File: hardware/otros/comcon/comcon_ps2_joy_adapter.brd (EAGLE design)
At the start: 50 x 50 mm, 44 parts

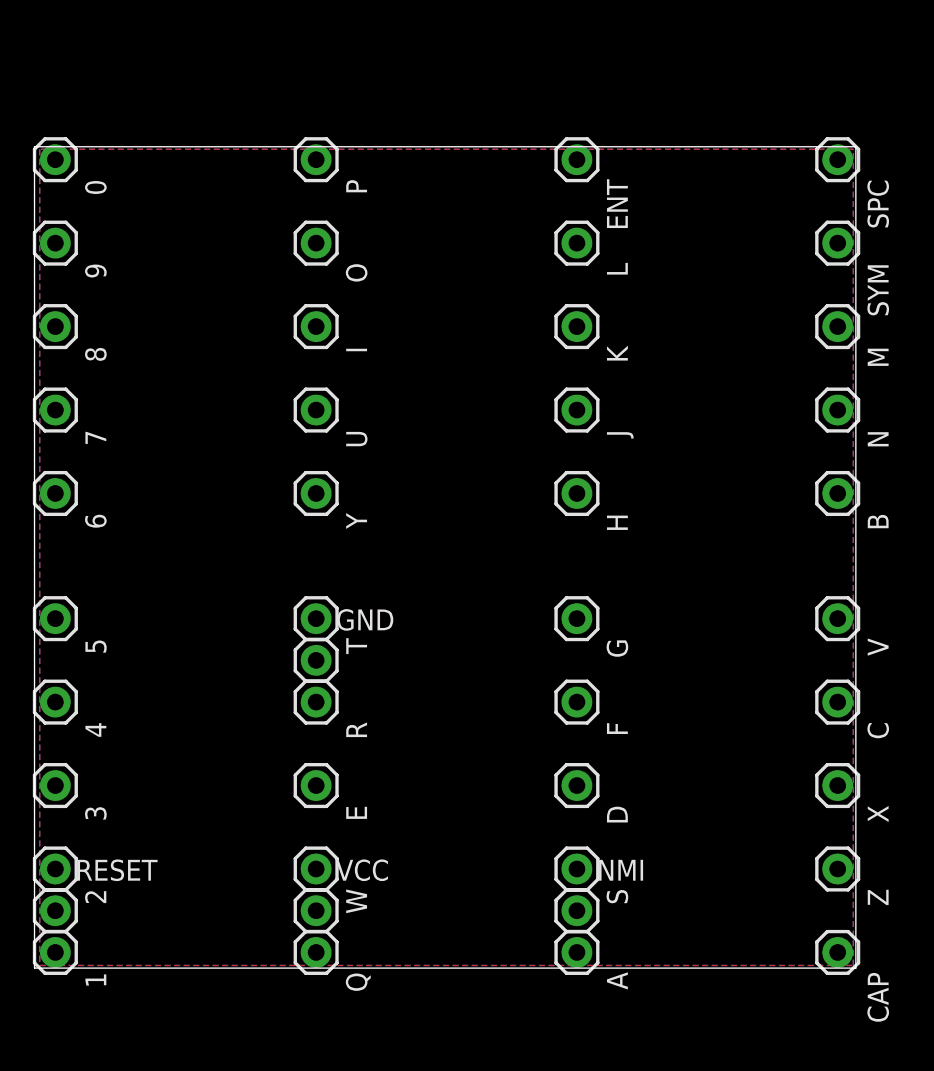
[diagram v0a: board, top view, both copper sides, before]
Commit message: 
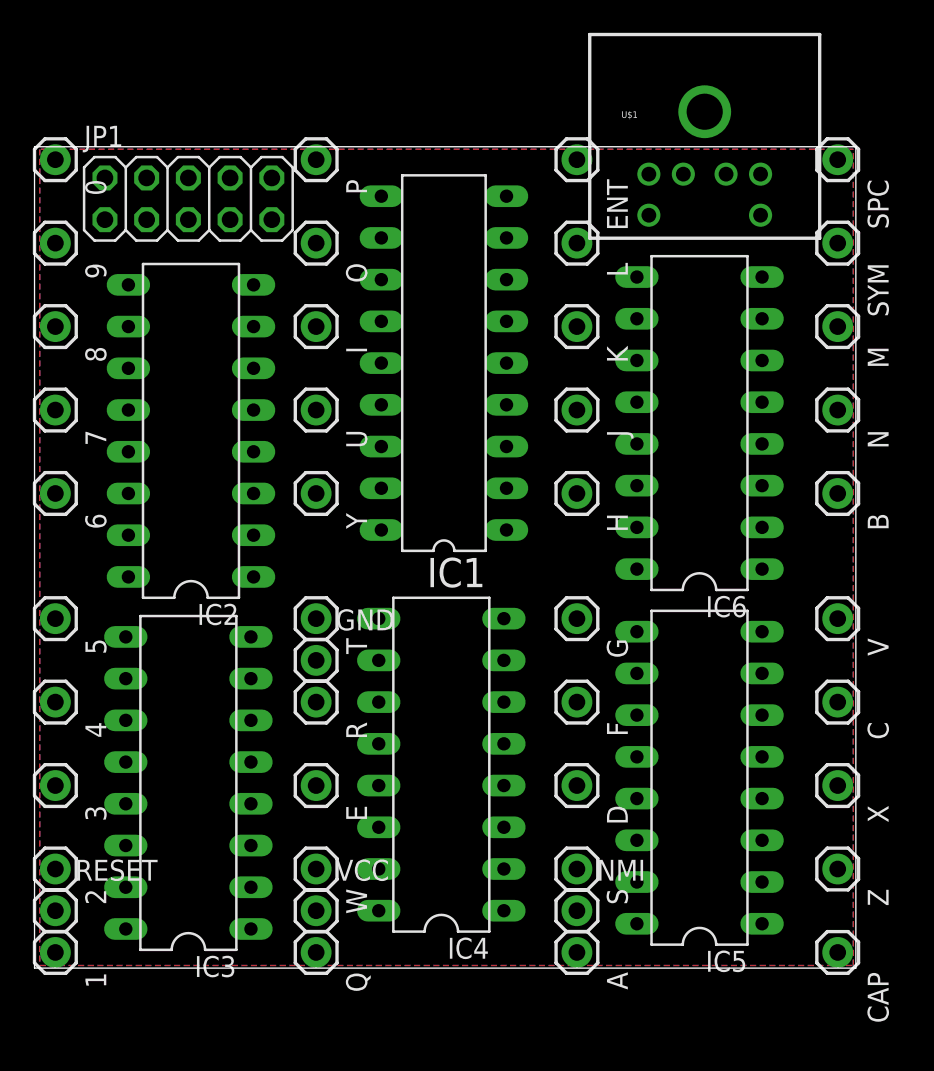
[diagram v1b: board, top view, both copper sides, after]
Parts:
- added IC1: PIC16F628P, microchip:DIL18
- added IC2, IC3, IC4, IC5, IC6: 74HC595N, 74xx-eu:DIL16
- added JP1: (no value), pinhead:2X05
- added U$1: MINI-DIN6PTH, SparkFun-Connectors:MINI-DIN6
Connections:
- removed net N$63: A.1
- removed net N$64: S.1
- new net N$1: A.1, IC2.5
- new net N$3: IC2.6, S.1
- new net N$4: IC2.9, IC3.14
- new net N$5: IC5.9, IC6.14
- new net N$6: IC3.9, IC4.14
- new net N$7: IC4.9, IC5.14
- new net VDD: IC1.14
- new net VSS: IC1.5
- net GND: now also IC2.8, IC3.8, IC4.8, IC5.8, IC6.8
- net N$105: now also IC4.15
- net N$106: now also IC4.1
- net N$107: now also IC4.2
- net N$108: now also IC4.3
- net N$12: now also IC6.1
- net N$18: now also IC6.2
- net N$2: now also IC6.15; no longer SPC.1
- net N$20: now also IC6.3
- net N$22: now also IC6.4
- net N$25: now also IC2.15
- net N$26: now also IC2.1
- net N$27: now also IC2.2
- net N$28: now also IC2.3
- net N$47: now also IC2.4
- net N$55: now also IC6.7
- net N$65: now also IC2.7
- net N$74: now also IC5.2; no longer P.1
- net N$75: now also IC5.3
- net N$76: now also IC5.4
- net N$77: now also IC5.5
- net N$78: now also IC5.6
- net N$84: now also IC3.2; no longer Q.1
- net N$85: now also IC3.3
- net N$86: now also IC3.4
- net N$87: now also IC3.5
- net N$88: now also IC3.6
- net N$94: now also IC5.7
- net N$95: now also IC4.7
- net N$96: now also IC4.6
- net N$97: now also IC4.5
- net N$98: now also IC4.4
- net VCC: now also IC2.16, IC3.16, IC4.16, IC5.16, IC6.16

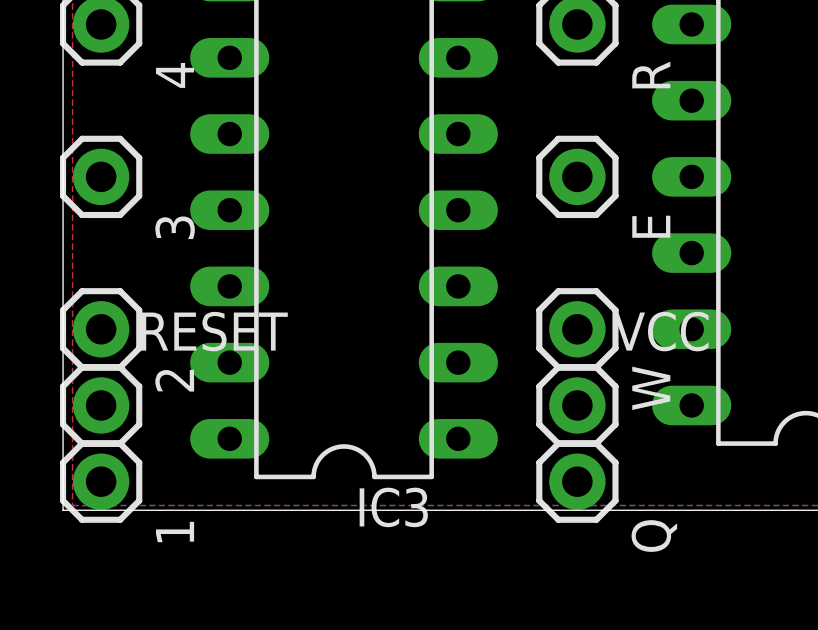
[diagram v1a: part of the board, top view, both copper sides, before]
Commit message: 
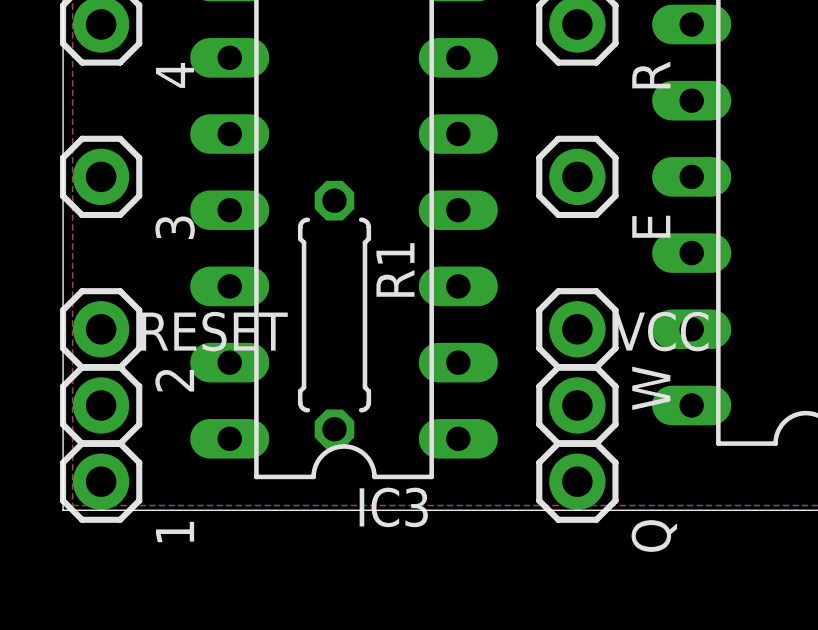
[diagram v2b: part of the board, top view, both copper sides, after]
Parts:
- added R1: 4K7, resistor:0207/7
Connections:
- removed net VSS: IC1.5
- new net N$8: IC1.4, JP1.1, R1.1
- new net RA0: IC2.12, IC3.12, IC4.12, IC5.12, IC6.12
- new net RA1: IC2.11, IC3.11, IC4.11, IC5.11, IC6.11
- new net RA2: IC2.14
- new net RB6: IC1.12
- new net RB7: IC1.13
- net GND: now also IC1.5, IC2.13, IC3.13, IC4.13, IC5.13, IC6.13, JP1.5
- net N$104: now also IC3.7
- net N$53: now also IC6.5
- net N$54: now also IC6.6
- net N$56: now also IC5.15
- net N$57: now also IC5.1
- net N$66: now also IC3.15
- net N$67: now also IC3.1
- net VCC: now also IC2.10, IC3.10, IC4.10, IC5.10, IC6.10, JP1.3, R1.2
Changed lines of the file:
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@@
 <element name="U$1" library="SparkFun-Connectors" package="MINI-DIN6" value="MINI-DIN6PTH" x="40.79875" y="56.8325"/>
 <element name="JP1" library="pinhead" package="2X05" value="" x="9.36625" y="46.83125"/>
+<element name="R1" library="resistor" package="0207/7" value="4K7" x="9.04875" y="6.50875" rot="R270"/>
 </elements>
 <signals>
@@
 <contactref element="IC5" pad="8"/>
 <contactref element="IC6" pad="8"/>
-<wire x1="44.29125" y1="20.47875" x2="44.29125" y2="42.06875" width="0" layer="19" extent="1-1"/>
-<wire x1="28.575" y1="21.2725" x2="44.29125" y2="20.47875" width="0" layer="19" extent="1-1"/>
-<wire x1="13.17625" y1="20.16125" x2="28.575" y2="21.2725" width="0" layer="19" extent="1-1"/>
-<wire x1="13.335" y1="41.5925" x2="13.17625" y2="20.16125" width="0" layer="19" extent="1-1"/>
-<wire x1="17.145" y1="18.7325" x2="13.335" y2="41.5925" width="0" layer="19" extent="1-1"/>
+<contactref element="IC3" pad="13"/>
+<contactref element="IC4" pad="13"/>
+<contactref element="IC5" pad="13"/>
+<contactref element="IC6" pad="13"/>
+<contactref element="IC2" pad="13"/>
+<contactref element="IC1" pad="5"/>
+<contactref element="JP1" pad="5"/>
+<wire x1="36.67125" y1="31.90875" x2="44.29125" y2="42.06875" width="0" layer="19" extent="1-1"/>
+<wire x1="28.73375" y1="36.83" x2="36.67125" y2="31.90875" width="0" layer="19" extent="1-1"/>
+<wire x1="28.575" y1="21.2725" x2="36.67125" y2="31.90875" width="0" layer="19" extent="1-1"/>
+<wire x1="17.145" y1="18.7325" x2="28.575" y2="21.2725" width="0" layer="19" extent="1-1"/>
+<wire x1="13.17625" y1="20.16125" x2="17.145" y2="18.7325" width="0" layer="19" extent="1-1"/>
+<wire x1="20.955" y1="11.1125" x2="17.145" y2="18.7325" width="0" layer="19" extent="1-1"/>
+<wire x1="5.55625" y1="10.00125" x2="13.17625" y2="20.16125" width="0" layer="19" extent="1-1"/>
+<wire x1="5.715" y1="31.4325" x2="13.17625" y2="20.16125" width="0" layer="19" extent="1-1"/>
+<wire x1="13.335" y1="41.5925" x2="5.715" y2="31.4325" width="0" layer="19" extent="1-1"/>
+<wire x1="9.36625" y1="45.56125" x2="13.335" y2="41.5925" width="0" layer="19" extent="1-1"/>
+<wire x1="36.67125" y1="10.31875" x2="28.575" y2="21.2725" width="0" layer="19" extent="1-1"/>
+<wire x1="44.29125" y1="20.47875" x2="36.67125" y2="10.31875" width="0" layer="19" extent="1-1"/>
 </signal>
 <signal name="VCC" class="1">
@@
 <contactref element="IC5" pad="16"/>
 <contactref element="IC6" pad="16"/>
-<wire x1="36.67125" y1="2.69875" x2="36.67125" y2="24.28875" width="0" layer="19" extent="1-1"/>
-<wire x1="20.955" y1="3.4925" x2="36.67125" y2="2.69875" width="0" layer="19" extent="1-1"/>
-<wire x1="5.55625" y1="2.38125" x2="20.955" y2="3.4925" width="0" layer="19" extent="1-1"/>
-<wire x1="5.715" y1="23.8125" x2="5.55625" y2="2.38125" width="0" layer="19" extent="1-1"/>
-<wire x1="17.145" y1="3.4925" x2="5.715" y2="23.8125" width="0" layer="19" extent="1-1"/>
+<contactref element="IC3" pad="10"/>
+<contactref element="IC4" pad="10"/>
+<contactref element="IC5" pad="10"/>
+<contactref element="IC6" pad="10"/>
+<contactref element="IC2" pad="10"/>
+<contactref element="JP1" pad="3"/>
+<contactref element="R1" pad="2"/>
+<wire x1="36.67125" y1="24.28875" x2="36.67125" y2="39.52875" width="0" layer="19" extent="1-1"/>
+<wire x1="36.67125" y1="17.93875" x2="36.67125" y2="24.28875" width="0" layer="19" extent="1-1"/>
+<wire x1="36.67125" y1="2.69875" x2="36.67125" y2="17.93875" width="0" layer="19" extent="1-1"/>
+<wire x1="20.955" y1="18.7325" x2="36.67125" y2="17.93875" width="0" layer="19" extent="1-1"/>
+<wire x1="20.955" y1="3.4925" x2="20.955" y2="18.7325" width="0" layer="19" extent="1-1"/>
+<wire x1="17.145" y1="3.4925" x2="20.955" y2="3.4925" width="0" layer="19" extent="1-1"/>
+<wire x1="5.55625" y1="2.38125" x2="17.145" y2="3.4925" width="0" layer="19" extent="1-1"/>
+<wire x1="9.04875" y1="2.69875" x2="5.55625" y2="2.38125" width="0" layer="19" extent="1-1"/>
+<wire x1="5.55625" y1="17.62125" x2="5.55625" y2="2.38125" width="0" layer="19" extent="1-1"/>
+<wire x1="5.715" y1="23.8125" x2="5.55625" y2="17.62125" width="0" layer="19" extent="1-1"/>
+<wire x1="5.715" y1="39.0525" x2="5.715" y2="23.8125" width="0" layer="19" extent="1-1"/>
+<wire x1="6.82625" y1="45.56125" x2="5.715" y2="39.0525" width="0" layer="19" extent="1-1"/>
 </signal>
 <signal name="N$2">
@@
 <signal name="N$54">
 <contactref element="L" pad="1"/>
+<contactref element="IC6" pad="6"/>
+<wire x1="33.02" y1="44.1325" x2="44.29125" y2="36.98875" width="0" layer="19" extent="1-1"/>
 </signal>
 <signal name="N$55">
@@
 <signal name="N$56">
 <contactref element="J" pad="1"/>
+<contactref element="IC5" pad="15"/>
+<wire x1="36.67125" y1="5.23875" x2="33.02" y2="33.9725" width="0" layer="19" extent="1-1"/>
 </signal>
 <signal name="N$57">
 <contactref element="H" pad="1"/>
+<contactref element="IC5" pad="1"/>
+<wire x1="44.29125" y1="2.69875" x2="33.02" y2="28.8925" width="0" layer="19" extent="1-1"/>
 </signal>
 <signal name="N$65">
@@
 <signal name="N$66">
 <contactref element="F" pad="1"/>
+<contactref element="IC3" pad="15"/>
+<wire x1="5.55625" y1="4.92125" x2="33.02" y2="16.1925" width="0" layer="19" extent="1-1"/>
 </signal>
 <signal name="N$67">
 <contactref element="G" pad="1"/>
+<contactref element="IC3" pad="1"/>
+<wire x1="13.17625" y1="2.38125" x2="33.02" y2="21.2725" width="0" layer="19" extent="1-1"/>
 </signal>
 <signal name="N$74">
@@
 <contactref element="NMI" pad="1"/>
 </signal>
-<signal name="VSS">
-<contactref element="IC1" pad="5"/>
-</signal>
 <signal name="VDD">
 <contactref element="IC1" pad="14"/>
@@
 <signal name="N$104">
 <contactref element="1" pad="1"/>
+<contactref element="IC3" pad="7"/>
+<wire x1="1.27" y1="0.9525" x2="13.17625" y2="17.62125" width="0" layer="19" extent="1-1"/>
 </signal>
 <signal name="N$4">
@@
 <signal name="N$53">
 <contactref element="ENT" pad="1"/>
+<contactref element="IC6" pad="5"/>
+<wire x1="44.29125" y1="34.44875" x2="33.02" y2="49.2125" width="0" layer="19" extent="1-1"/>
 </signal>
 <signal name="N$5">
@@
 <wire x1="36.67125" y1="20.47875" x2="36.67125" y2="29.36875" width="0" layer="19" extent="1-1"/>
 </signal>
+<signal name="RA0">
+<contactref element="IC2" pad="12"/>
+<contactref element="IC3" pad="12"/>
+<contactref element="IC4" pad="12"/>
+<contactref element="IC5" pad="12"/>
+<contactref element="IC6" pad="12"/>
+<wire x1="36.67125" y1="12.85875" x2="36.67125" y2="34.44875" width="0" layer="19" extent="1-1"/>
+<wire x1="20.955" y1="13.6525" x2="36.67125" y2="12.85875" width="0" layer="19" extent="1-1"/>
+<wire x1="5.55625" y1="12.54125" x2="20.955" y2="13.6525" width="0" layer="19" extent="1-1"/>
+<wire x1="5.715" y1="33.9725" x2="5.55625" y2="12.54125" width="0" layer="19" extent="1-1"/>
+</signal>
+<signal name="RA1">
+<contactref element="IC2" pad="11"/>
+<contactref element="IC3" pad="11"/>
+<contactref element="IC4" pad="11"/>
+<contactref element="IC5" pad="11"/>
+<contactref element="IC6" pad="11"/>
+<wire x1="36.67125" y1="15.39875" x2="36.67125" y2="36.98875" width="0" layer="19" extent="1-1"/>
+<wire x1="20.955" y1="16.1925" x2="36.67125" y2="15.39875" width="0" layer="19" extent="1-1"/>
+<wire x1="5.55625" y1="15.08125" x2="20.955" y2="16.1925" width="0" layer="19" extent="1-1"/>
+<wire x1="5.715" y1="36.5125" x2="5.55625" y2="15.08125" width="0" layer="19" extent="1-1"/>
+</signal>
+<signal name="RA2">
+<contactref element="IC2" pad="14"/>
+</signal>
+<signal name="N$8">
+<contactref element="IC1" pad="4"/>
+<contactref element="JP1" pad="1"/>
+<contactref element="R1" pad="1"/>
+<wire x1="4.28625" y1="45.56125" x2="28.73375" y2="34.29" width="0" layer="19" extent="1-1"/>
+<wire x1="9.04875" y1="10.31875" x2="28.73375" y2="34.29" width="0" layer="19" extent="1-1"/>
+</signal>
+<signal name="RB6">
+<contactref element="IC1" pad="12"/>
+</signal>
+<signal name="RB7">
+<contactref element="IC1" pad="13"/>
+</signal>
 </signals>
